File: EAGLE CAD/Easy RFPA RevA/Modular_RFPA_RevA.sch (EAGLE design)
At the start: 197 parts, among them IC401 LDO_3TERMMC78M12CTGTO220_VERT, IC402 LDO_3TERMMC78M05CTGTO220_VERT, J401 FUSE_2P, J402 KK_PCFAN, Q101 IRF520N, Q102 IRF630, Q201 IRF630, Q202 IRF630, Q301 MOSFET_NBSS123SOT23, Q302 PNPSOT23_BEC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

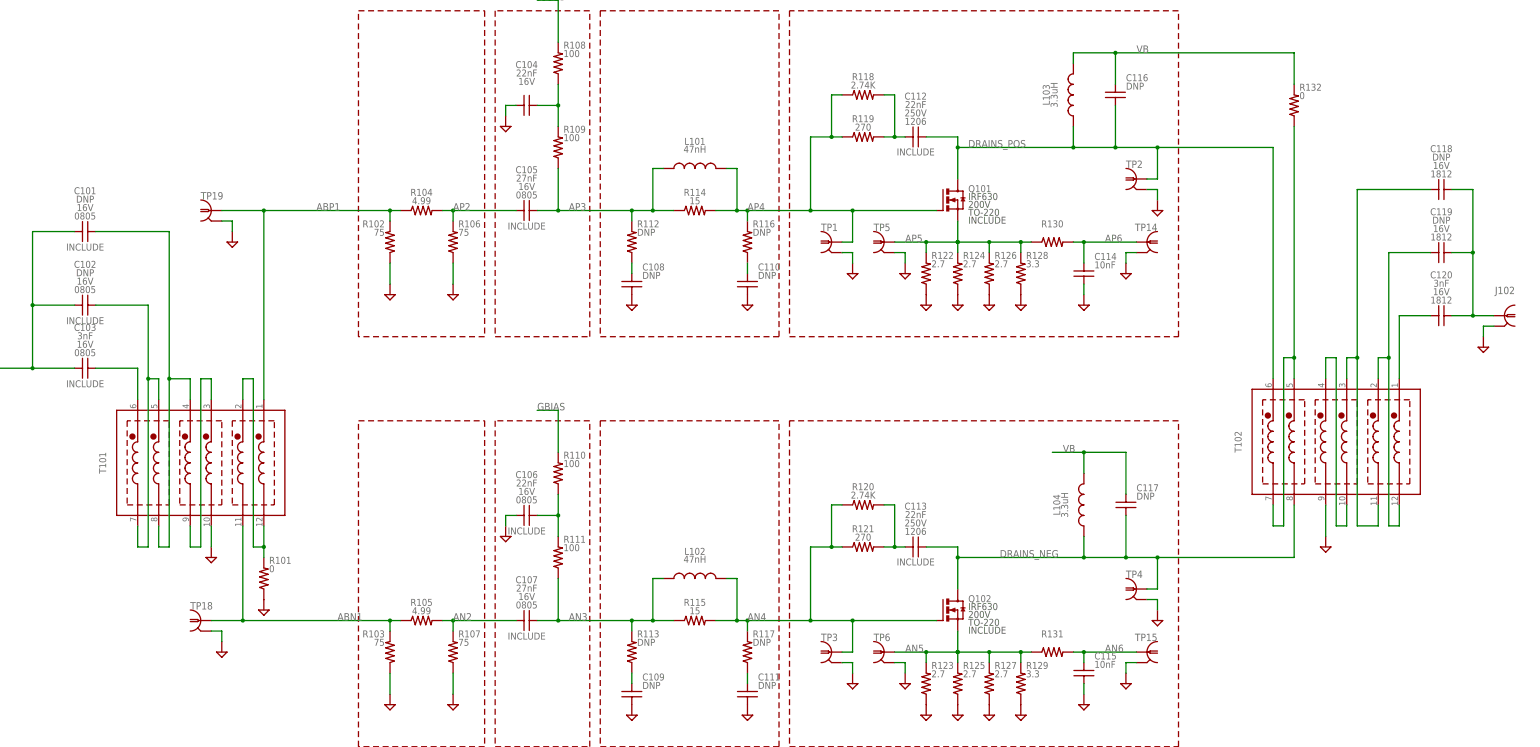
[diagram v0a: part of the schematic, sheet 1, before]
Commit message: Do same for capacitor library
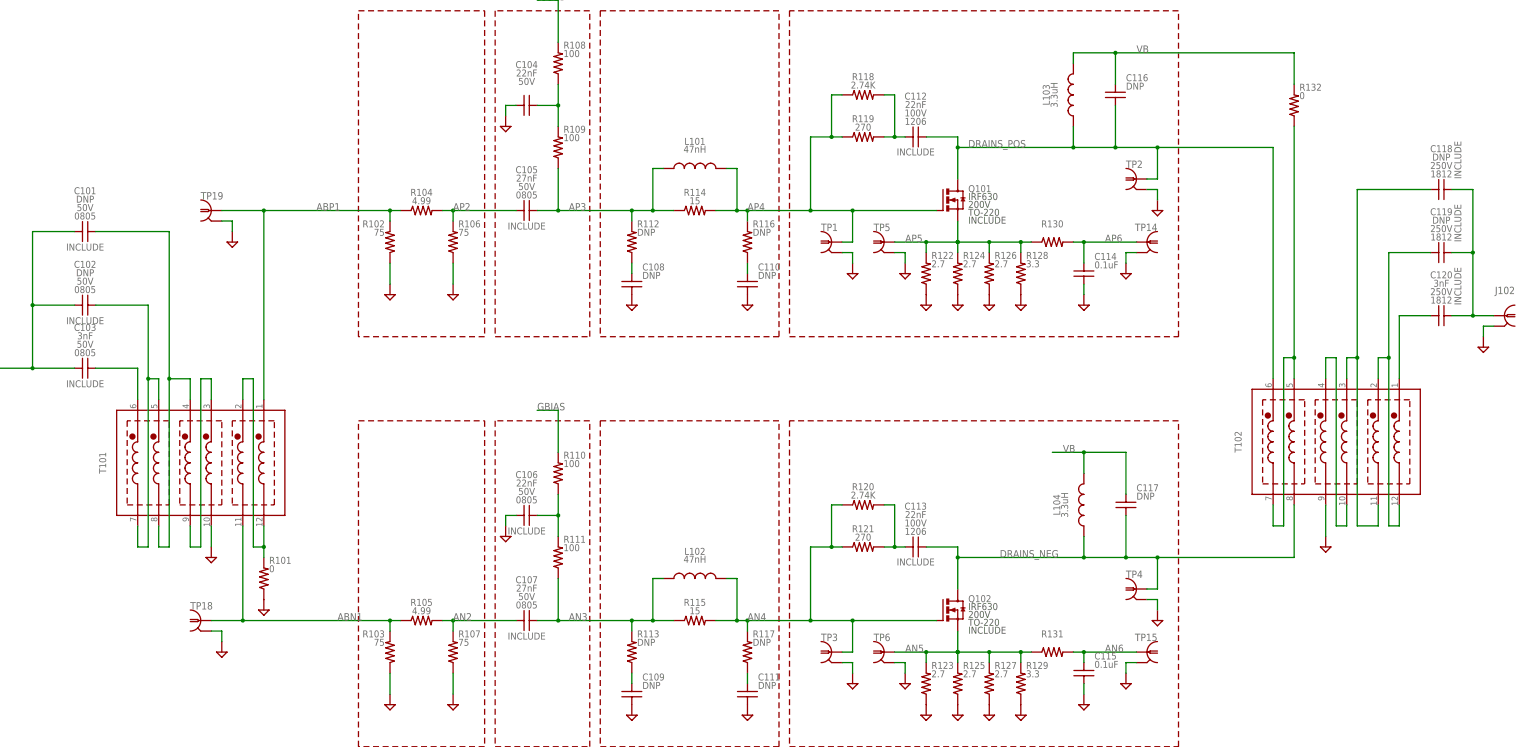
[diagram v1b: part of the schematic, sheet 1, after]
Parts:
- C101, C102, C103, C104, C105, C106, C107: device MDT_C:CC-0.1U-16V-0805-X7R0805_IPC -> MDT_C:CGEN0805_IPC; BOM INCLUDE -> (none); VOLTAGE (none) -> 50V
- C108, C109, C110, C111: device MDT_C:CC-0.1U-16V-0805-X7R0805_IPC -> MDT_C:CGEN0805_IPC; VOLTAGE (none) -> 50V
- C112, C113: device MDT_C:CC-22N-250V-5%-1206-NP0C1206 -> MDT_C:CGENC1206; VOLTAGE (none) -> 100V
- C114, C115: value 10nF -> 0.1uF; device MDT_C:CC-0.1U-16V-0805-X7R0805_IPC -> MDT_C:CGEN0805_IPC; VOLTAGE (none) -> 50V
- C116, C117: device MDT_C:CC1812 -> MDT_C:CGENC1812; VOLTAGE (none) -> 100V
- C118, C119, C120: device MDT_C:CC1812 -> MDT_C:CGENC1812; VOLTAGE (none) -> 250V
- C201, C203: value 22nF -> 0.1uF
- C202, C204: value 27nF -> 0.1uF
- C205, C206, C207, C208, C302, C303: value DNP -> 0.1uF
- C211, C212: value 10nF -> 0.1uF
- C304: value 33pF -> 0.1uF

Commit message: More part attributes....
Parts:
- removed X401: (no value), con-wago-500:W237-102
- added J1: HDR_2X1282836-1282836-1, MDT_CON:HDR_2X1282836-1282836-1
- C101, C102, C108, C109, C110, C111, C116, C117, C118, C119, R112, R113, R116, R117, R211, R212, R215, R216, R311: BOM (none) -> EXCLUDE
- C114, C115: value 0.1uF -> 10nF
- C201, C203: value 0.1uF -> 22nF; device MDT_C:CC-0.1U-16V-0805-X7R0805_IPC -> MDT_C:CGEN0805_IPC; BOM INCLUDE -> (none); VOLTAGE (none) -> 50V
- C202, C204: value 0.1uF -> 27nF; device MDT_C:CC-0.1U-16V-0805-X7R0805_IPC -> MDT_C:CGEN0805_IPC; BOM INCLUDE -> (none); VOLTAGE (none) -> 50V
- C205, C206, C207, C208: value 0.1uF -> DNP; device MDT_C:CC-0.1U-16V-0805-X7R0805_IPC -> MDT_C:CGEN0805_IPC; BOM (none) -> EXCLUDE; VOLTAGE (none) -> 50V
- C209, C210: value 22nF -> 2.2nF; device MDT_C:CC-22N-250V-5%-1206-NP0C1206 -> MDT_C:CGENC1206; VOLTAGE (none) -> 100V
- C211, C212: value 0.1uF -> 10nF; device MDT_C:CC-0.1U-16V-0805-X7R0805_IPC -> MDT_C:CGEN0805_IPC; VOLTAGE (none) -> 50V
- C301, C305, C306: device MDT_C:CC-0.1U-16V-0805-X7R0805_IPC -> MDT_C:CGEN0805_IPC; VOLTAGE (none) -> 25V
- C302: value 0.1uF -> DNP; device MDT_C:CC-0.1U-16V-0805-X7R0805_IPC -> MDT_C:CGEN0805_IPC; BOM INCLUDE -> EXCLUDE; VOLTAGE (none) -> 25V
- C303: value 0.1uF -> DNP; device MDT_C:CC-0.1U-16V-0805-X7R0805_IPC -> MDT_C:CGEN0805_IPC; BOM (none) -> EXCLUDE; VOLTAGE (none) -> 25V
- C304: value 0.1uF -> 33pF; device MDT_C:CC-0.1U-16V-0805-X7R0805_IPC -> MDT_C:CGEN0805_IPC; VOLTAGE (none) -> 50V
- C403, C404: device MDT_C:CCC-6.8U-50V-10%-1210-X7SC1210 -> MDT_C:CGENC1210
- C406, C407: value 47nF -> 4.7uF; device MDT_C:CC-47N-100V-5%-1206-NP0C1206 -> MDT_C:CGENC1206
- J101, J102, J301, J302: value (none) -> COAX112640BNC_EDGE; device MDT_CON:COAXBNC_EDGE -> MDT_CON:COAX112640BNC_EDGE
- R130, R131: value (none) -> 10K
- R301: device rcl:R-TRIMM3299W -> MDT_R:RTRIMRTRIM-10K-10%-3299W-0.5W3299W
- R302, R303, R304, R305, R306, R308, R310, R312, R315, R316, R317: device MDT_R:RGEN0805_IPC -> MDT_R:R90GEN0805_IPC
- R313: device MDT_R:RGEN0805_IPC -> MDT_R:R90GEN0805_IPC; BOM (none) -> EXCLUDE
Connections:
- net GND: now also J1.2; no longer X401-2.KL
- net N$45: now also J1.1; no longer X401-1.KL
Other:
- moved on the sheet: R302, R303, R304, R305, R306, R308, R310, R312, R313, R315, R316, R317

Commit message: EXCLUDEs and INCLUDEs
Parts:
- C403, C404: DIALECTRIC (none) -> X7S; VOLTAGE (none) -> 50V
- C406, C407: DIALECTRIC (none) -> X7R; VOLTAGE (none) -> 50V
- H401, H402, H403, H404: BOM (none) -> EXCLUDE
- renumbered IC401 to U401, IC402 to U402
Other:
- note removed: "Heatsink"
- moved on the sheet: C101, C102, C103, C114, C115, C118, C119, C120, C401, C402, C405, C408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

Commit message: bom-ex export working
Need to use tab-delimited format due to parts with commas in partno....
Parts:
- R130, R131: value 10K -> 1K
- U301: BOM (none) -> INCLUDE; DESCRIPTION (none) -> IC INVERT SCHMITT 1CH 1-IN SOT25; PACKAGE (none) -> SOT23-5; PARTNO (none) -> 74AHC1G14QW5-7; VENDOR (none) -> Diodes Inc
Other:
- note removed: "Gate Bias Generator"
- moved on the sheet: C101, C102, C103, C104, C105, C106, C107, C108, C109, C110, C111, C112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

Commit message: Tidying up revA schematic
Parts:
- removed J1: HDR_2X1282836-1282836-1, MDT_CON:HDR_2X1282836-1282836-1
- added F401: FUSE_2P, MDT_FUSE:FUSE_2P
- J401: value FUSE_2P -> HDR_2X1282836-1282836-1; device MDT_FUSE:FUSE_2P -> MDT_CON:HDR_2X1282836-1282836-1
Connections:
- net GND: now also J401.2; no longer J1.2
- net N$44: now also F401.2; no longer J401.2
- net N$45: now also F401.1; no longer J1.1
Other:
- note added: "! Caution !! Current design lacks advanced self-protection features! User is responsible for limiting unblanking duty cycle and bias voltage/current Current design is tested under following conditions: Supply voltage VB: 48V Bias current: 3.1A (in each FET) Max duty cycle: 3.5% (500us, 70Hz rep rate, passive convection) Max pulse width: 1ms"
- note added: "Attenuator"
- note added: "Bias T"
- note added: "Connector for 12V fan Caution, limit current to 0.2A!"
- note added: "Damped LC filter"
- note added: "Gate damping"
- note added: "Heatsink"
- note added: "If not using analog input, Then short out jumpers JP1 and JP2"
- note added: "Input balun"
- note added: "Input protection Intended for 48VDC supply Should work with 35-50VDC"
- note added: "Linear regulators"
- note added: "Mounting holes"
- note added: "Output balun"
- note added: "Power FET"
- note added: "To drain bias"
- note added: "Unblanking input Active High, TTL logic"
- note removed: "Circuit: * C:\Workspace\Git\BASIC_MRI_RFPA\LTSPICE simulations\RFPA_IRF630_pushpullx2_tran_param.asc Direct Newton iteration for .op point succeeded. pep: 50=(33.9794dB,0°) vd: 48=(33.6248dB,0°) vdmin: 12=(21.5836dB,0°) rload_lv_se_target: 12.96=(22.2521dB,0°) rload_lv_se: 12.96=(22.2521dB,0°) idmin: 0.5=(-6.0206dB,0°) id: 3.27777777777778=(10.3116dB,0°) gm0: 3.54=(10.9801dB,0°) gm: 1=(0dB,0°) rs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"
- note removed: "If not using analog bias tracking Then short out jumpers JP1 and JP2"
- note removed: "Unblanking input"
- note removed: "for preamp stage using one pair of IRF520N pep: 10=(20dB,0°) vd: 48=(33.6248dB,0°) vdmin: 26=(28.2995dB,0°) rload_lv_se_target: 24.2=(27.6763dB,0°) rload_lv_se: 24.2=(27.6763dB,0°) idmin: 0.5=(-6.0206dB,0°) id: 1.40909090909091=(2.97878dB,0°) gm0: 5.7=(15.1175dB,0°) gm: 0.5=(-6.0206dB,0°) rs: 1.82456140350877=(5.22317dB,0°) rgbias: 100=(40dB,0°) rsource_lv_se: 25=(27.9588dB,0°) rfb: 246.2=(47.825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"
